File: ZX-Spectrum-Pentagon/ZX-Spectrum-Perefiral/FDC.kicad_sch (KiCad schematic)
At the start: 57 parts

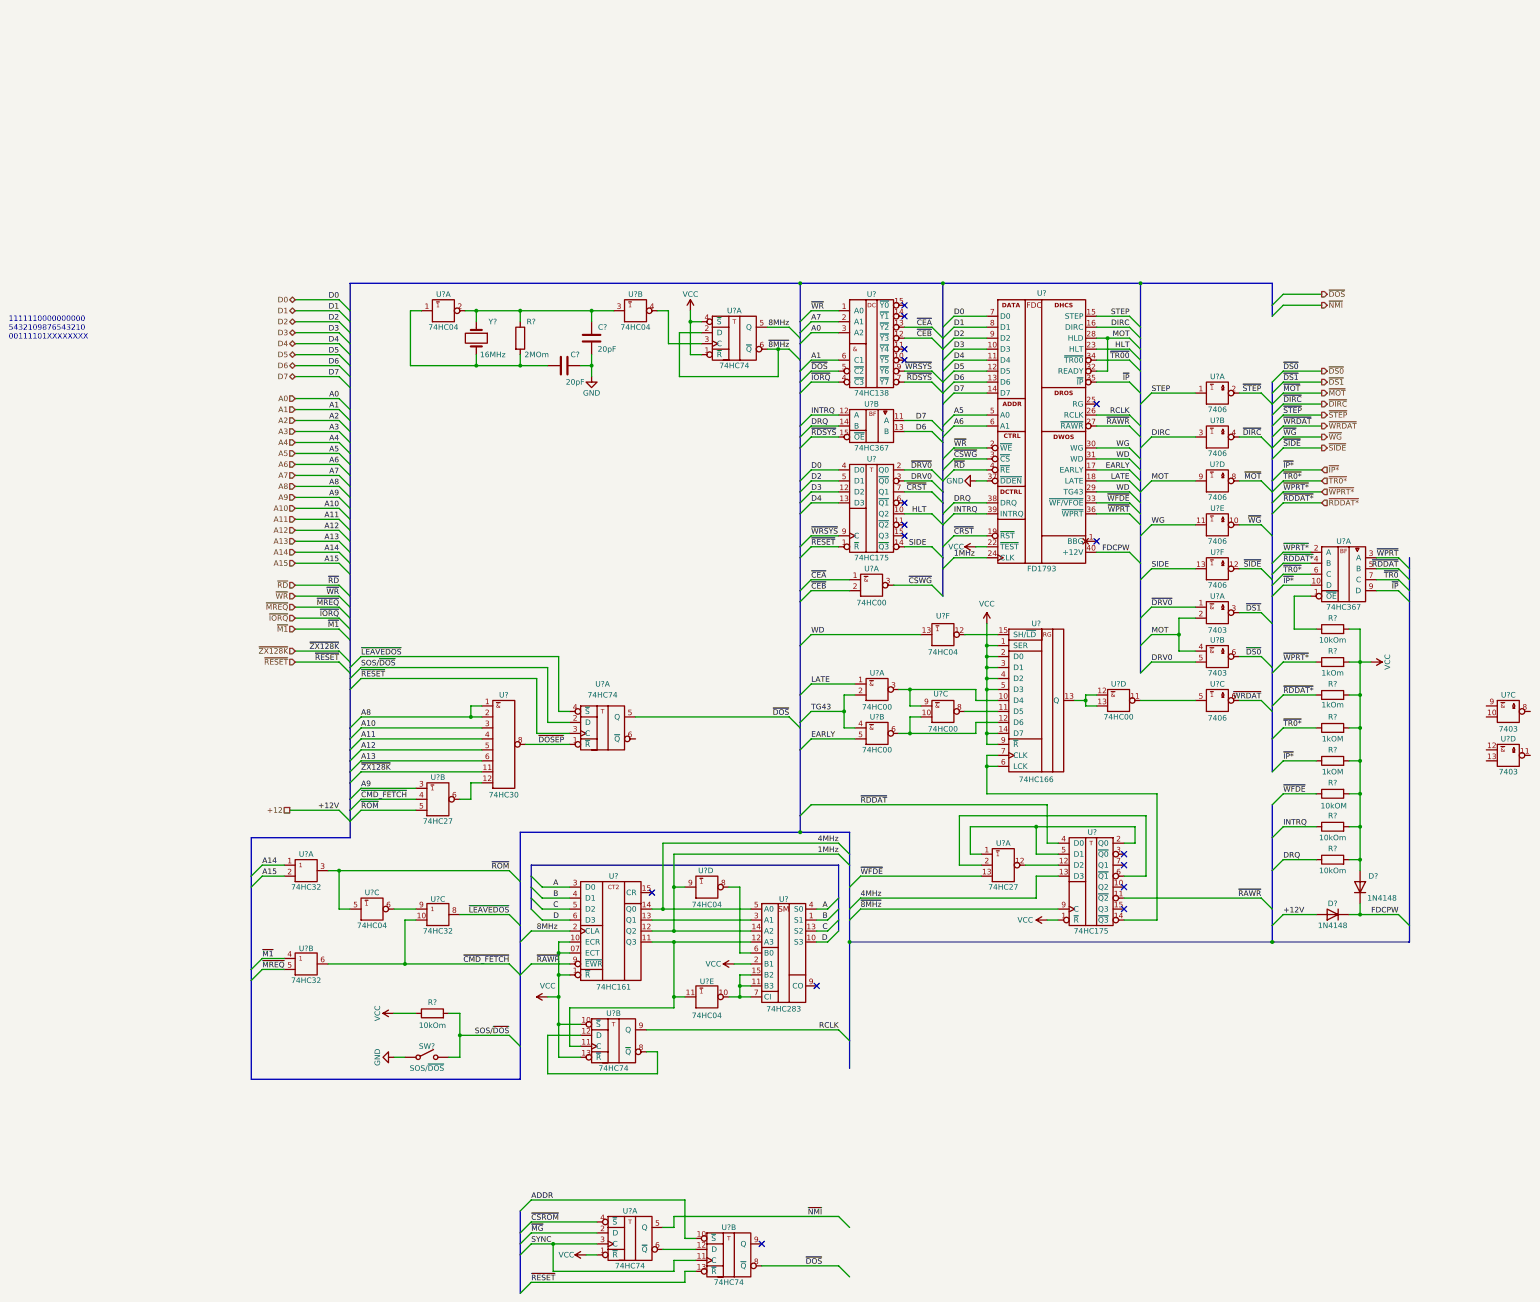
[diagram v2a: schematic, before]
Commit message: update keyboard & FDC schematic
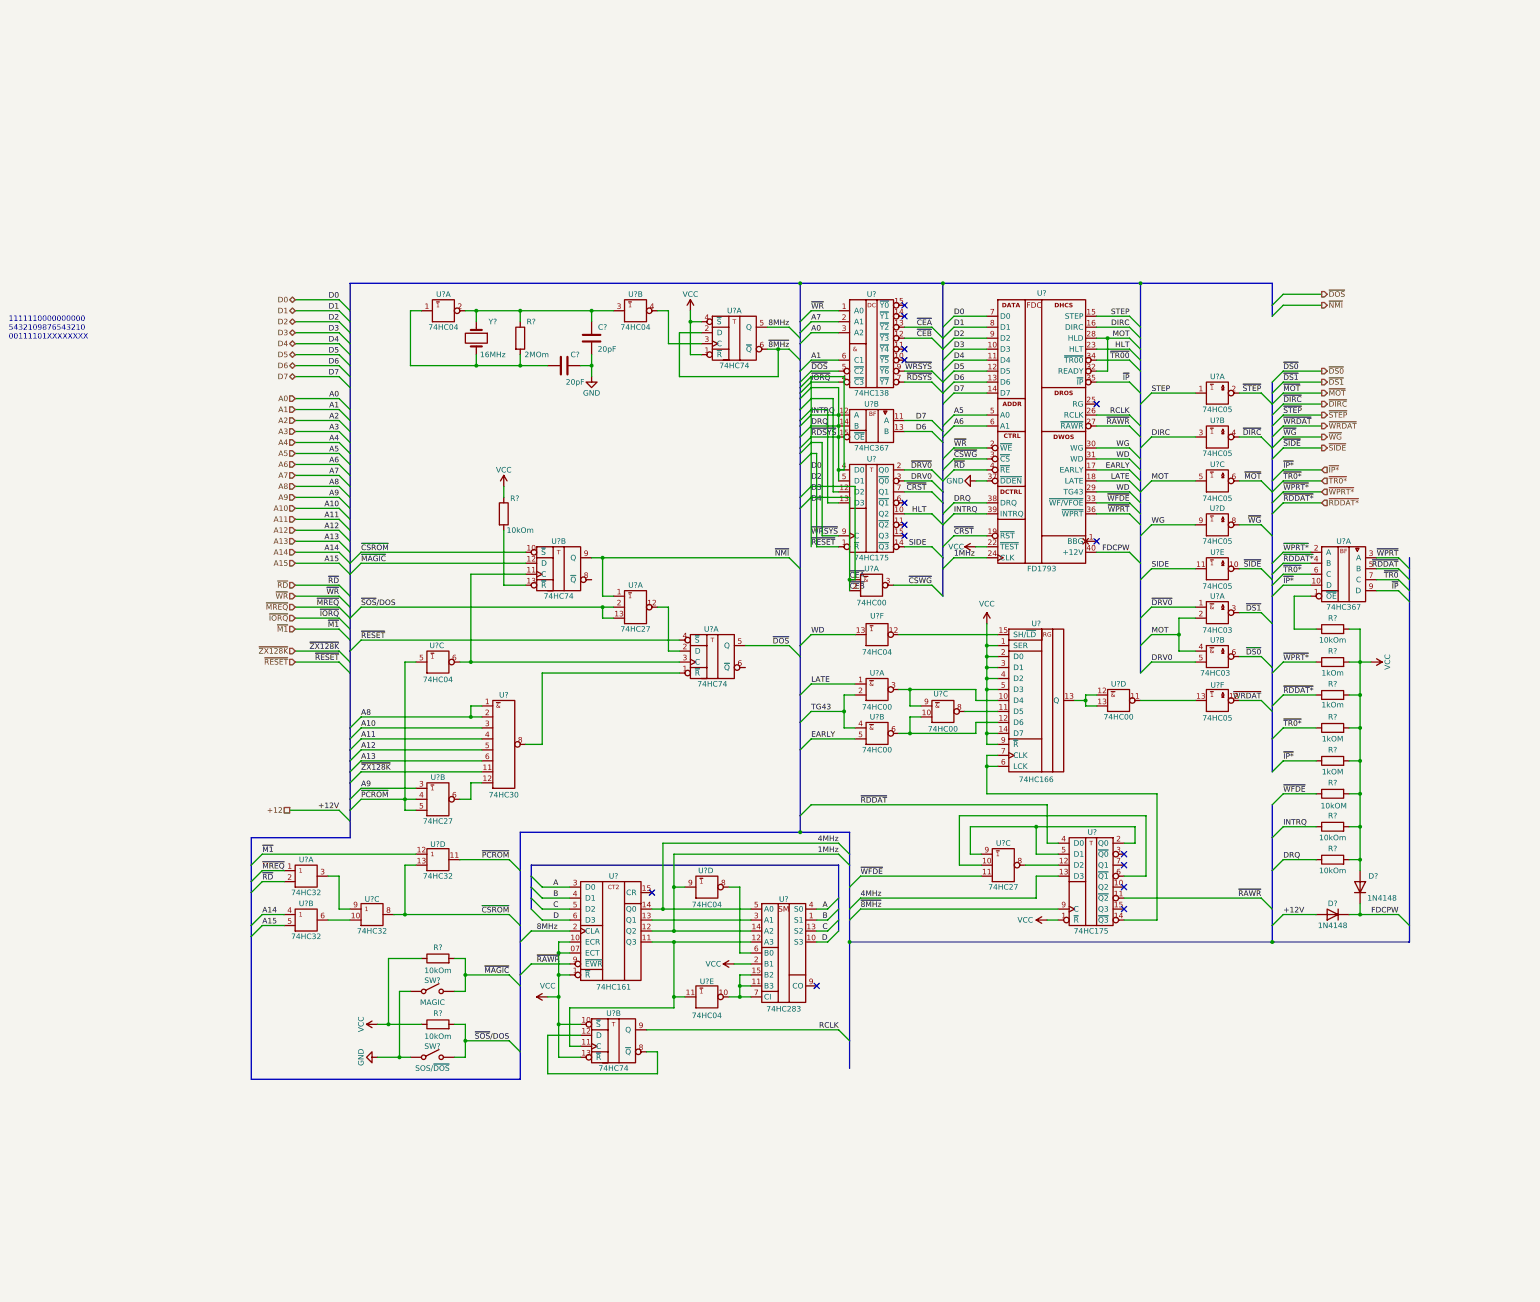
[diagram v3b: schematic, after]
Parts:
- removed U? (x4): 7403, Package_DIP:DIP-16_W7.62mm, symbol 74IEC:7403
- removed U? (x3): 74HC74, Package_DIP:DIP-14_W7.62mm, symbol 74IEC:74HC74
- removed U?: 74HC32, Package_DIP:DIP-14_W7.62mm, symbol 74IEC:74HC32
- removed U? (x6): 7406, Package_DIP:DIP-16_W7.62mm, symbol 74IEC:7406
- removed U?: 74HC04, Package_DIP:DIP-14_W7.62mm, symbol 74IEC:74HC04
- added R? (x2): 10kOm, Resistor_SMD:R_0805_2012Metric_Pad1.20x1.40mm_HandSolder, symbol Device:R
- added SW?: MAGIC, symbol Switch:SW_SPST
- added U? (x6): 74HC05, symbol 74IEC:74HC05
- added U? (x2): 74HC32, Package_DIP:DIP-14_W7.62mm, symbol 74IEC:74HC32
- added U? (x2): 74HC03, symbol 74IEC:74HC03
- added U? (x2): 74HC74, Package_DIP:DIP-14_W7.62mm, symbol 74IEC:74HC74
- added U?: 74HC27, Package_DIP:DIP-14_W7.62mm, symbol 74IEC:74HC27
- added U?: 74HC04, Package_DIP:DIP-14_W7.62mm, symbol 74IEC:74HC04
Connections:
- net D2 is gone; now on net D0: U?.5 (D1), U?.9 (D2)
- net D3 is gone; now on net D0: U?.10 (D3), U?.12 (D2)
- net D4 is gone; now on net D0: U?.11 (D4), U?.13 (D3)
- net DRQ is gone; now on net D0: R?.1, U?.14 (B), U?.38 (DRQ)
- net INTRQ is gone; now on net D0: R?.1, U?.12 (A), U?.39 (INTRQ)
- net ~{CEA} is gone; now on net D0: U?.1 (A), U?.13 (~{Y2})
- net ~{CEB} is gone; now on net D0: U?.12 (~{Y3}), U?.2 (B)
- net ~{IORQ} is gone; now on net D0: U?.4 (~{C3})
- net ~{LEAVEDOS} is gone; now on net ~{CSROM}: U?.8 (Y)
- net ~{RDSYS} is gone; now on net D0: U?.15 (~{OE}), U?.7 (~{Y7})
- net ~{RESET} is gone; now on net D0: U?.1 (~{R})
- net ~{WRSYS} is gone; now on net D0: U?.9 (C), U?.9 (~{Y6})
- net A14: now also U?.4 (A); no longer U?.1 (A)
- net A15: now also U?.5 (B); no longer U?.2 (B)
- net D0: now also U?.4 (~{S})
- net DIRC: now also U?.3 (A)
- net DRV0: now also U?.5 (B)
- net GND: now also SW?.1 (A), U?.10 (GND), U?.7 (GND), U?.7 (GND), U?.7 (GND), U?.7 (GND), U?.7 (GND), U?.7 (GND), U?.7 (GND), U?.7 (GND), U?.7 (GND), U?.7 (GND), U?.7 (GND), U?.7 (GND), U?.7 (GND)
- net MOT: now also U?.2 (B), U?.4 (A), U?.5 (A)
- net SIDE: now also U?.11 (A)
- net STEP: now also U?.1 (A)
- net VCC: now also R?.1, R?.1, U?.14 (VCC), U?.14 (VCC), U?.14 (VCC), U?.14 (VCC), U?.14 (VCC), U?.14 (VCC), U?.14 (VCC), U?.14 (VCC), U?.14 (VCC), U?.14 (VCC), U?.14 (VCC), U?.14 (VCC), U?.14 (VCC), U?.14 (VCC)
- net WG: now also U?.9 (A)
- net ~{CSROM}: now also U?.10 (~{S}), U?.13 (B)
- net ~{DIRC}: now also U?.4 (~{Y})
- net ~{DOS}: now also U?.5 (Q)
- net ~{DRV0}: now also U?.1 (A)
- net ~{DS0}: now also U?.6 (~{Y})
- net ~{DS1}: now also U?.3 (~{Y})
- net ~{M1}: now also U?.12 (A)
- net ~{MOT}: now also U?.6 (~{Y})
- net ~{MREQ}: now also U?.1 (A)
- net ~{NMI}: now also U?.1 (A), U?.9 (Q)
- net ~{RD}: now also U?.2 (B)
- net ~{SIDE}: now also U?.10 (~{Y})
- net ~{STEP}: now also U?.2 (~{Y})
- net ~{WFDE}: now also U?.11 (C); no longer U?.13 (C)
- net ~{WG}: now also U?.8 (~{Y})
- net ~{WRDAT}: now also U?.12 (~{Y})
- net at U?.9 (A): now also U?.3 (Y)
- net at U?.12 (D2): now also U?.8 (~{Y}); no longer U?.12 (~{Y})
- net at U?.2 (Q0), U?.5 (D1): now also U?.9 (A); no longer U?.1 (A)
- net at U?.6 (~{Q1}): now also U?.10 (B); no longer U?.2 (B)
- net at U?.11 (~{Y}): now also U?.13 (A)
- net SOS/~{DOS} renamed ~{SOS}/DOS
- net ~{SOS}/DOS: now also U?.13 (C), U?.2 (B)
- net ~{CMD_FETCH}: no longer names the net of U?.10 (B)
- net ~{CMD_FETCH}: now also U?.6 (Y); no longer U?.4 (B)
- net ~{DOSEP}: no longer names the net of U?.8 (~{Y})
- net ~{DOSEP}: now also U?.1 (~{R})
- net ~{ROM} renamed ~{PCROM}
- net ~{PCROM}: now also U?.4 (B), U?.11 (Y), U?.5 (A); no longer U?.3 (Y)
- new net: R?.2, U?.13 (~{R})
- new net: U?.11 (C), U?.3 (C), U?.6 (~{Y})
- new net: U?.12 (~{Y}), U?.2 (D)
- new net ~{MAGIC}: R?.2, SW?.2 (B), U?.12 (D)
- no-connect marks 16 -> 15
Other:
- moved on the sheet: R?, SW?, U?A, U?C, U?F

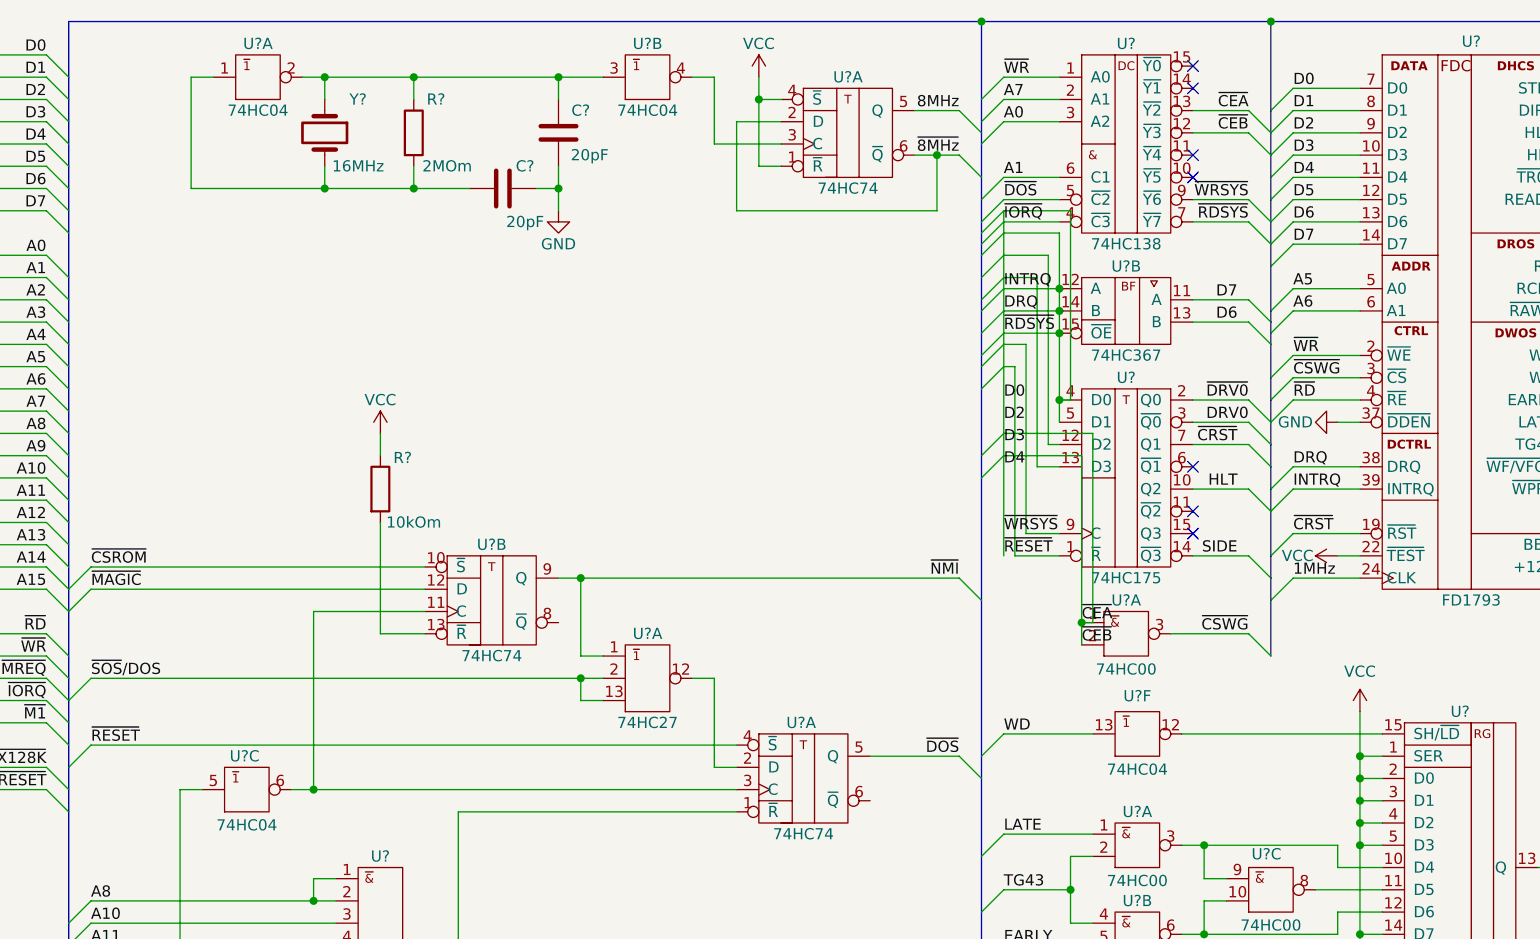
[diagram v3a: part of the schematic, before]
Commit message: restore schematic of FDC
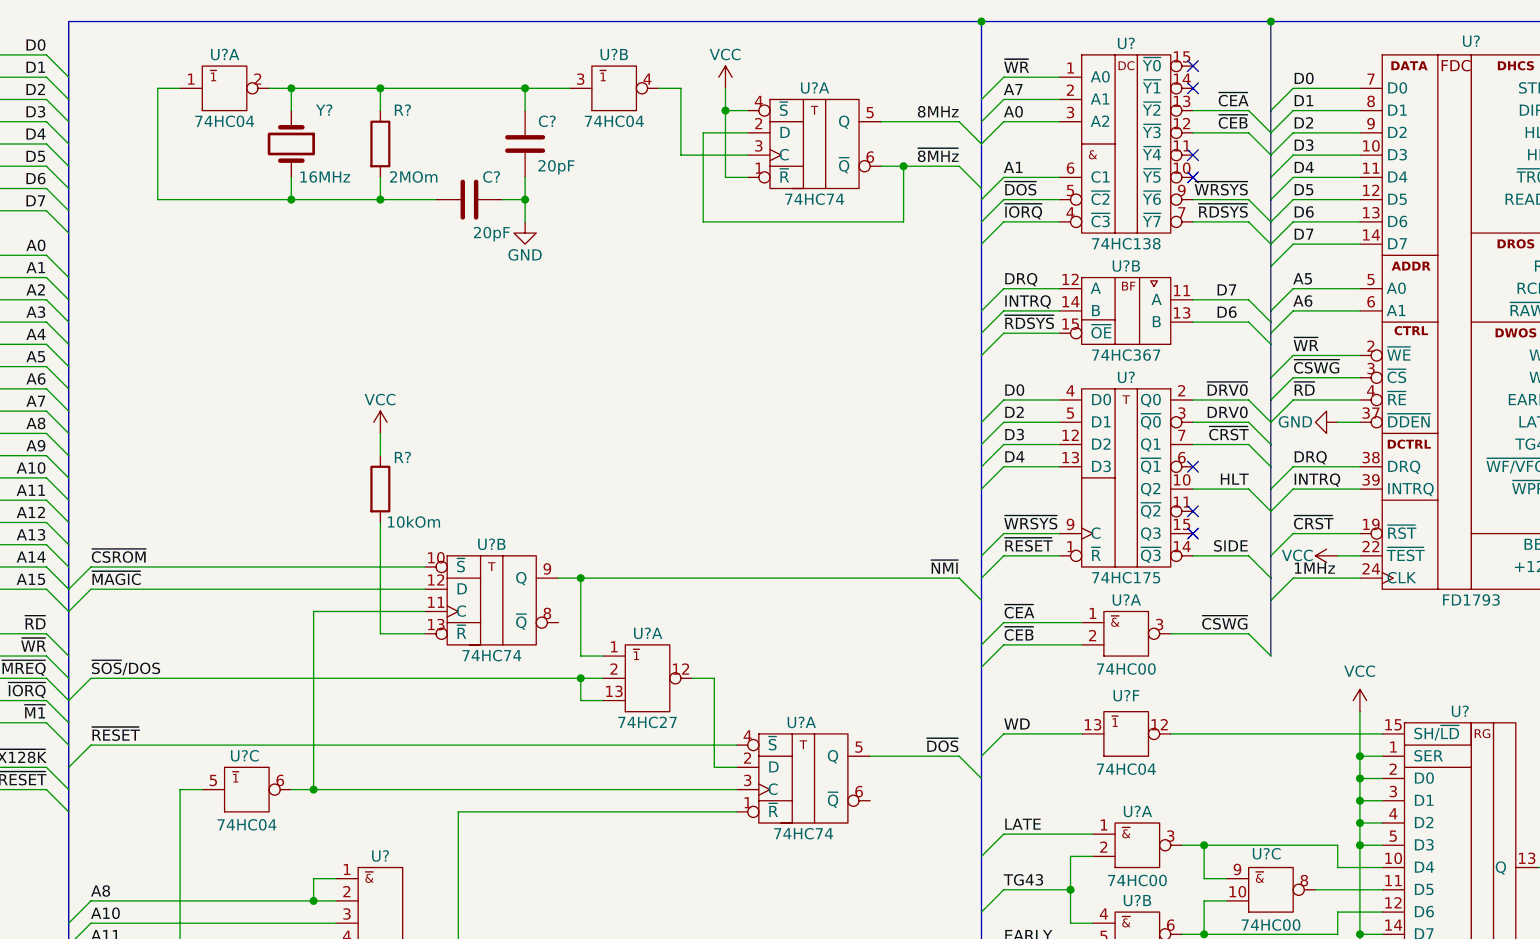
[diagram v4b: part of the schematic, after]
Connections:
- net D0: no longer R?.1, R?.1, U?.1 (A), U?.1 (~{R}), U?.10 (D3), U?.11 (D4), U?.12 (A), U?.12 (D2), U?.12 (~{Y3}), U?.13 (D3), U?.13 (~{Y2}), U?.14 (B), U?.15 (~{OE}), U?.2 (B), U?.38 (DRQ), U?.39 (INTRQ), U?.4 (~{C3}), U?.4 (~{S}), U?.5 (D1), U?.7 (~{Y7}), U?.9 (C), U?.9 (D2), U?.9 (~{Y6})
- new net D2: U?.5 (D1), U?.9 (D2)
- new net D3: U?.10 (D3), U?.12 (D2)
- new net D4: U?.11 (D4), U?.13 (D3)
- new net DRQ: R?.1, U?.12 (A), U?.38 (DRQ)
- new net INTRQ: R?.1, U?.14 (B), U?.39 (INTRQ)
- new net ~{CEA}: U?.1 (A), U?.13 (~{Y2})
- new net ~{CEB}: U?.12 (~{Y3}), U?.2 (B)
- new net ~{IORQ}: U?.4 (~{C3})
- new net ~{RDSYS}: U?.15 (~{OE}), U?.7 (~{Y7})
- new net ~{RESET}: U?.1 (~{R}), U?.4 (~{S})
- new net ~{WRSYS}: U?.9 (C), U?.9 (~{Y6})
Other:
- moved on the sheet: C?, R?, U?A, U?B, U?F, Y?

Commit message: update ZX-Spectrum-Perefiral
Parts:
- removed U?: 74HC00, Package_DIP:DIP-16_W7.62mm, symbol 74IEC:74HC00
- added R7: 1kOM, Resistor_SMD:R_0805_2012Metric, symbol Device:R
- added unit 3 of U10
- gave numbers to parts that had none: 36
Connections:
- net EARLY: now also U8.13 (B); no longer U8.5 (B)
- net GND: now also U10.7 (GND)
- net LATE: now also U8.4 (A); no longer U8.1 (A)
- net TG43: now also U8.12 (A), U8.5 (B); no longer U8.2 (B), U8.4 (A)
- net VCC: now also R7.1, U10.14 (VCC)
- net at U12.10 (D4), U8.9 (A): now also U8.6 (~{Y}); no longer U8.3 (~{Y})
- net at U12.12 (D6), U8.10 (B): now also U8.11 (~{Y}); no longer U8.6 (~{Y})
- net at U12.13 (Q): now also U10.10 (B), U10.9 (A)
- net at U4.13 (A): now also R7.2, U10.8 (~{Y})
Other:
- moved on the sheet: U1F, U8A
